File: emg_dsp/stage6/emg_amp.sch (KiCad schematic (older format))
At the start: 17 parts, among them U83 OPA4348, U84 MAX4208

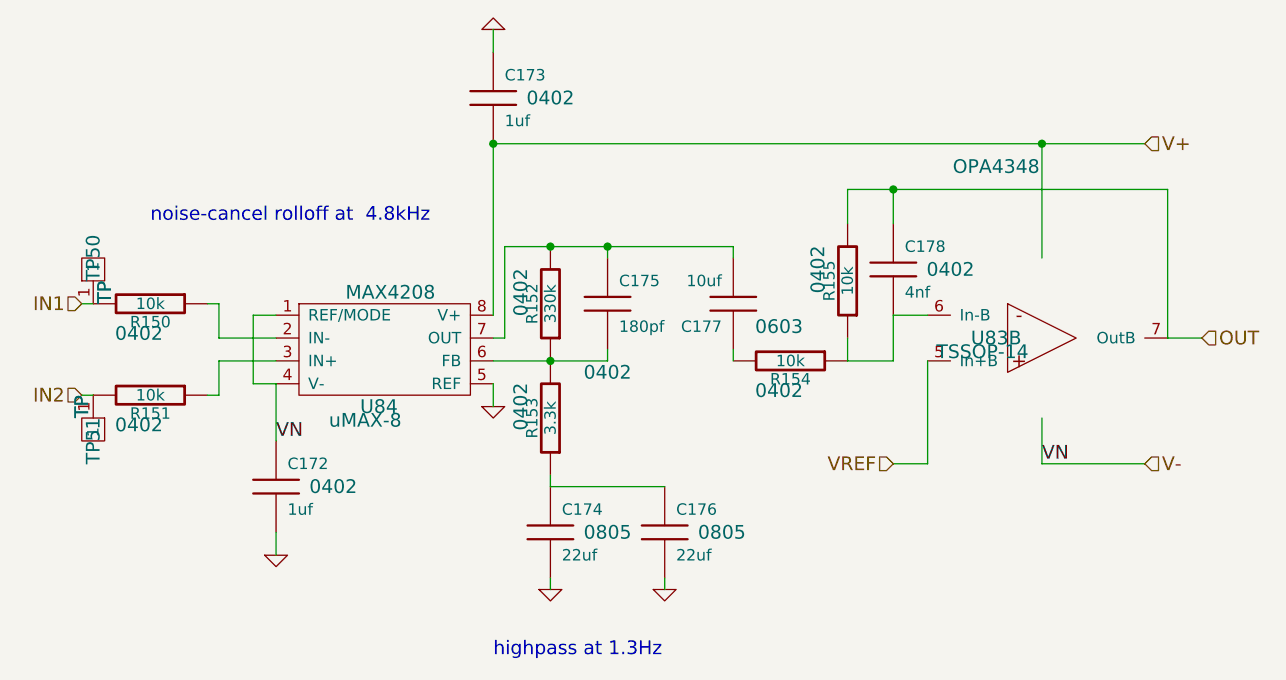
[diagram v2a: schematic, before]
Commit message: wired, wireless, some of bridge are routed. next up is the EMG system.
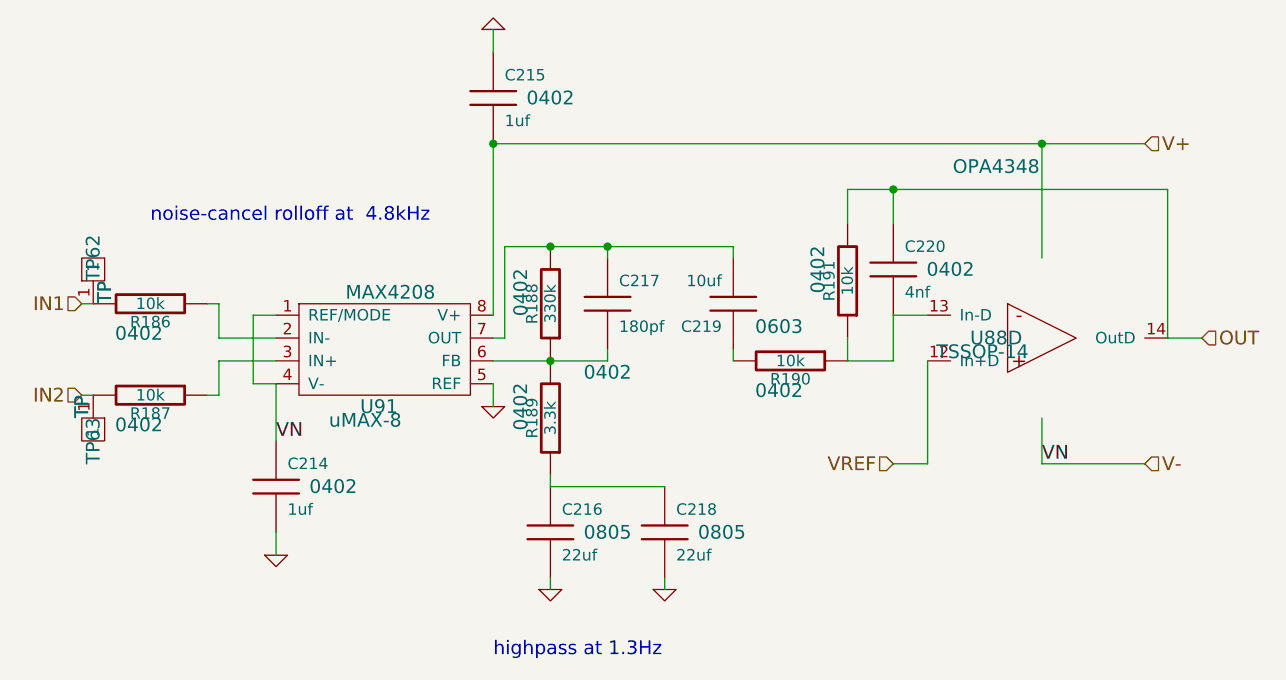
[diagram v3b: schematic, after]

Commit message: getting closer -- needt o put DACs on the board so we can listen to the emg / neural data!
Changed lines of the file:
@@
-EESchema Schematic File Version 2  date Wed 29 Sep 2010 05:47:59 PM EDT
+EESchema Schematic File Version 2  date Thu 30 Sep 2010 12:31:09 AM EDT
 LIBS:power
 LIBS:device
@@
 Sheet 10 13
 Title "Stage 4 / Copyright 2010 Timothy L Hanson "
-Date "29 sep 2010"
+Date "30 sep 2010"
 Rev ""
 Comp "This design is free: redistribute or modify under the GPL v. 3 or later"
@@
 AR Path="/4C9BA165/4C9D6BC0/4C9D733B" Ref="TP53"  Part="1"
 AR Path="/4C9BA165/4C9D5FEB/4C9D733B" Ref="TP49"  Part="1"
-F 0 "TP63" H 1950 4000 60  0000 C CNN
+F 0 "TP55" H 1950 4000 60  0000 C CNN
 F 1 "TP" H 1800 3950 60  0000 C CNN
 F 2 "TP" H 1800 3950 60  0000 C CNN
@@
 AR Path="/4C9BA165/4C9D6BC0/4C9D732E" Ref="TP52"  Part="1"
 AR Path="/4C9BA165/4C9D5FEB/4C9D732E" Ref="TP48"  Part="1"
-F 0 "TP62" H 1950 3200 60  0000 C CNN
+F 0 "TP54" H 1950 3200 60  0000 C CNN
 F 1 "TP" H 1800 3150 60  0000 C CNN
 F 2 "TP" H 1800 3150 60  0000 C CNN
@@
 AR Path="/4C9BA165/4C9D6BC0/4C9D6A40" Ref="U83"  Part="3"
 AR Path="/4C9BA165/4C9D5FEB/4C9D6A40" Ref="U83"  Part="1"
-F 0 "U88" H 5900 3550 60  0000 C CNN
+F 0 "U83" H 5900 3550 60  0000 C CNN
 F 1 "OPA4348" H 5900 4300 60  0000 C CNN
 F 2 "TSSOP-14" H 5840 3490 60  0000 C CNN
@@
 AR Path="/4C9BA165/4C9D6BC0/4C9D684F" Ref="#PWR0261"  Part="1"
 AR Path="/4C9BA165/4C9D5FEB/4C9D684F" Ref="#PWR0266"  Part="1"
-F 0 "#PWR0266" H 4450 4650 30  0001 C CNN
+F 0 "#PWR0256" H 4450 4650 30  0001 C CNN
 F 1 "GND" H 4450 4580 30  0001 C CNN
 	1    4450 4650
@@
 AR Path="/4C9BA165/4C9D6BC0/4C9D6849" Ref="#PWR0262"  Part="1"
 AR Path="/4C9BA165/4C9D5FEB/4C9D6849" Ref="#PWR0267"  Part="1"
-F 0 "#PWR0267" H 3950 4650 30  0001 C CNN
+F 0 "#PWR0257" H 3950 4650 30  0001 C CNN
 F 1 "GND" H 3950 4580 30  0001 C CNN
 	1    3950 4650
@@
 AR Path="/4C9BA165/4C9D6BC0/4C9D6843" Ref="#PWR0263"  Part="1"
 AR Path="/4C9BA165/4C9D5FEB/4C9D6843" Ref="#PWR0268"  Part="1"
-F 0 "#PWR0268" H 2750 4500 30  0001 C CNN
+F 0 "#PWR0258" H 2750 4500 30  0001 C CNN
 F 1 "GND" H 2750 4430 30  0001 C CNN
 	1    2750 4500
@@
 AR Path="/4C9BA165/4C9D6BC0/4C9D681F" Ref="#PWR0264"  Part="1"
 AR Path="/4C9BA165/4C9D5FEB/4C9D681F" Ref="#PWR0269"  Part="1"
-F 0 "#PWR0269" H 3700 3850 30  0001 C CNN
+F 0 "#PWR0259" H 3700 3850 30  0001 C CNN
 F 1 "GND" H 3700 3780 30  0001 C CNN
 	1    3700 3850
@@
 AR Path="/4C9BA165/4C9D6BC0/4C9D67F5" Ref="#PWR0265"  Part="1"
 AR Path="/4C9BA165/4C9D5FEB/4C9D67F5" Ref="#PWR0270"  Part="1"
-F 0 "#PWR0270" H 3700 2200 30  0001 C CNN
+F 0 "#PWR0260" H 3700 2200 30  0001 C CNN
 F 1 "GND" H 3700 2130 30  0001 C CNN
 	1    3700 2200
@@
 AR Path="/4C9BA165/4C9D6BC0/4B607777" Ref="C184"  Part="1"
 AR Path="/4C9BA165/4C9D5FEB/4B607777" Ref="C170"  Part="1"
-F 0 "C219" H 4800 3500 50  0000 L CNN
+F 0 "C191" H 4800 3500 50  0000 L CNN
 F 1 "10uf" H 4800 3300 50  0000 L CNN
 F 2 "0603" H 4550 3500 60  0000 C CNN
@@
 AR Path="/4C9BA165/4C9D6BC0/4B5E8316" Ref="C180"  Part="1"
 AR Path="/4C9BA165/4C9D5FEB/4B5E8316" Ref="C166"  Part="1"
-F 0 "C215" H 3750 2600 50  0000 L CNN
+F 0 "C187" H 3750 2600 50  0000 L CNN
 F 1 "1uf" H 3750 2400 50  0000 L CNN
 F 2 "0402" H 3950 2500 60  0000 C CNN
@@
 AR Path="/4C9BA165/4C9D6BC0/4B5E82D0" Ref="C179"  Part="1"
 AR Path="/4C9BA165/4C9D5FEB/4B5E82D0" Ref="C165"  Part="1"
-F 0 "C214" H 2800 4300 50  0000 L CNN
+F 0 "C186" H 2800 4300 50  0000 L CNN
 F 1 "1uf" H 2800 4100 50  0000 L CNN
 F 2 "0402" H 3000 4200 60  0000 C CNN
@@
 AR Path="/4C9BA165/4C9D6BC0/4B5E2EEF" Ref="C185"  Part="1"
 AR Path="/4C9BA165/4C9D5FEB/4B5E2EEF" Ref="C171"  Part="1"
-F 0 "C220" H 5500 3350 50  0000 L CNN
+F 0 "C192" H 5500 3350 50  0000 L CNN
 F 1 "4nf" H 5500 3150 50  0000 L CNN
 F 2 "0402" H 5700 3250 60  0000 C CNN
@@
 AR Path="/4C9BA165/4C9D6BC0/4B5E2EB2" Ref="R161"  Part="1"
 AR Path="/4C9BA165/4C9D5FEB/4B5E2EB2" Ref="R149"  Part="1"
-F 0 "R191" V 5330 3300 50  0000 C CNN
+F 0 "R167" V 5330 3300 50  0000 C CNN
 F 1 "10k" V 5250 3300 50  0000 C CNN
 F 2 "0402" V 5380 3250 60  0000 C CNN
@@
 AR Path="/4C9BA165/4C9D6BC0/4B5E2EA6" Ref="R160"  Part="1"
 AR Path="/4C9BA165/4C9D5FEB/4B5E2EA6" Ref="R148"  Part="1"
-F 0 "R190" V 5080 3650 50  0000 C CNN
+F 0 "R166" V 5080 3650 50  0000 C CNN
 F 1 "10k" V 5000 3650 50  0000 C CNN
 F 2 "0402" V 5130 3600 60  0000 C CNN
@@
 AR Path="/4C9BA165/4C9D6BC0/4B5E2BEE" Ref="C183"  Part="1"
 AR Path="/4C9BA165/4C9D5FEB/4B5E2BEE" Ref="C169"  Part="1"
-F 0 "C218" H 4500 4500 50  0000 L CNN
+F 0 "C190" H 4500 4500 50  0000 L CNN
 F 1 "22uf" H 4500 4300 50  0000 L CNN
 F 2 "0805" H 4700 4400 60  0000 C CNN
@@
 AR Path="/4C9BA165/4C9D6BC0/4B5E2631" Ref="C182"  Part="1"
 AR Path="/4C9BA165/4C9D5FEB/4B5E2631" Ref="C168"  Part="1"
-F 0 "C217" H 4250 3500 50  0000 L CNN
+F 0 "C189" H 4250 3500 50  0000 L CNN
 F 1 "180pf" H 4250 3300 50  0000 L CNN
 F 2 "0402" H 4200 3100 60  0000 C CNN
@@
 AR Path="/4C9BA165/4C9D6BC0/4B5E2425" Ref="C181"  Part="1"
 AR Path="/4C9BA165/4C9D5FEB/4B5E2425" Ref="C167"  Part="1"
-F 0 "C216" H 4000 4500 50  0000 L CNN
+F 0 "C188" H 4000 4500 50  0000 L CNN
 F 1 "22uf" H 4000 4300 50  0000 L CNN
 F 2 "0805" H 4200 4400 60  0000 C CNN
@@
 AR Path="/4C9BA165/4C9D6BC0/4B5E23F1" Ref="R158"  Part="1"
 AR Path="/4C9BA165/4C9D5FEB/4B5E23F1" Ref="R146"  Part="1"
-F 0 "R188" V 4030 3400 50  0000 C CNN
+F 0 "R164" V 4030 3400 50  0000 C CNN
 F 1 "330k" V 3950 3400 50  0000 C CNN
 F 2 "0402" V 4080 3350 60  0000 C CNN
@@
 AR Path="/4C9BA165/4C9D6BC0/4B5E23EA" Ref="R159"  Part="1"
 AR Path="/4C9BA165/4C9D5FEB/4B5E23EA" Ref="R147"  Part="1"
-F 0 "R189" V 4030 3900 50  0000 C CNN
+F 0 "R165" V 4030 3900 50  0000 C CNN
 F 1 "3.3k" V 3950 3900 50  0000 C CNN
 F 2 "0402" V 4080 3850 60  0000 C CNN
@@
 AR Path="/4C9BA165/4C9D6BC0/4B5E2389" Ref="R157"  Part="1"
 AR Path="/4C9BA165/4C9D5FEB/4B5E2389" Ref="R145"  Part="1"
-F 0 "R187" V 2280 3800 50  0000 C CNN
+F 0 "R163" V 2280 3800 50  0000 C CNN
 F 1 "10k" V 2200 3800 50  0000 C CNN
 F 2 "0402" V 2330 3750 60  0000 C CNN
@@
 AR Path="/4C9BA165/4C9D6BC0/4B5E236D" Ref="R156"  Part="1"
 AR Path="/4C9BA165/4C9D5FEB/4B5E236D" Ref="R144"  Part="1"
-F 0 "R186" V 2280 3400 50  0000 C CNN
+F 0 "R162" V 2280 3400 50  0000 C CNN
 F 1 "10k" V 2200 3400 50  0000 C CNN
 F 2 "0402" V 2330 3350 60  0000 C CNN
@@
 AR Path="/4C9BA165/4C9D6BC0/4B5E2341" Ref="U85"  Part="1"
 AR Path="/4C9BA165/4C9D5FEB/4B5E2341" Ref="U82"  Part="1"
-F 0 "U91" H 3200 3350 60  0000 C CNN
+F 0 "U86" H 3200 3350 60  0000 C CNN
 F 1 "MAX4208" H 3250 3850 60  0000 C CNN
 F 2 "uMAX-8" H 3140 3290 60  0000 C CNN
